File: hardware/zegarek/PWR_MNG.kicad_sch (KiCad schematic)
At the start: 14 parts, among them J1 Conn_01x02_Socket, J2 Conn_01x02_Pin, Q1 IRF740, U1 MC34063AD

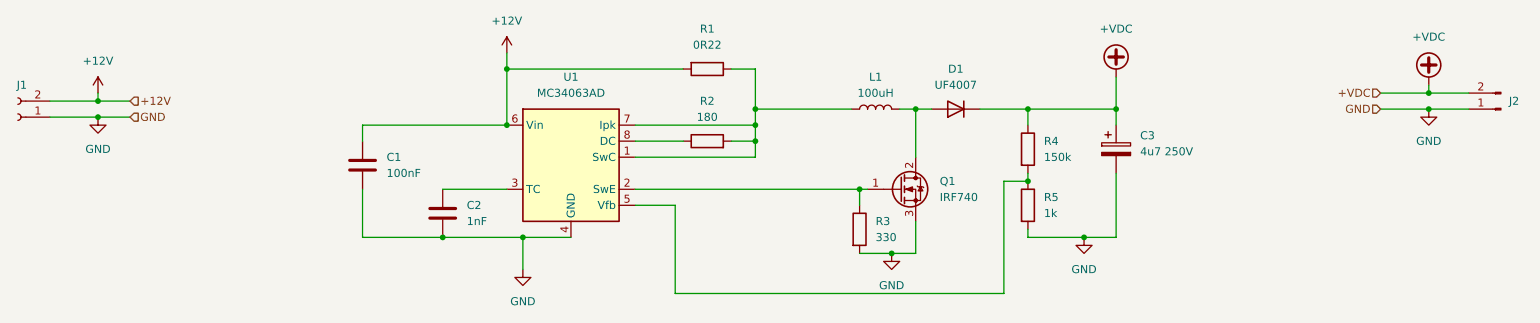
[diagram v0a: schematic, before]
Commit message: page MCU and NIXIE done, nixiepwr changed name to PWR MNG
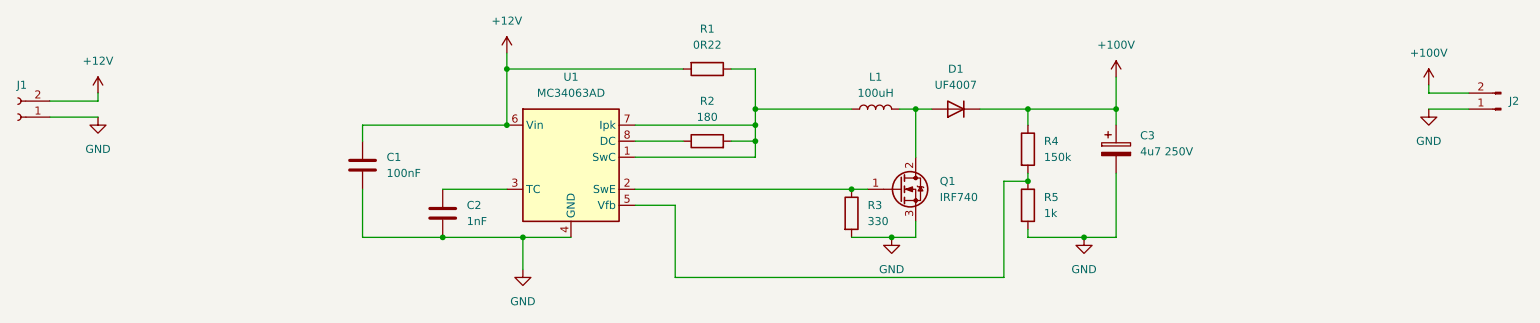
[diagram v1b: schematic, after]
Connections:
- net +VDC renamed +100V
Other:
- moved on the sheet: R3

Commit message: pwr page done
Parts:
- removed J1: Conn_01x02_Socket, Connector:Banana_Jack_2Pin, symbol Connector:Conn_01x02_Socket
- added C22, C25: 0.33u, symbol Device:C_Small
- added C23, C24: 100n, symbol Device:C_Small
- added J6: Barrel_Jack_MountingPin, Connector_BarrelJack:BarrelJack_Wuerth_694106106102_2.0x5.5mm, symbol Connector:Barrel_Jack_MountingPin
- added U8: DI78L3.3UAB, Package_TO_SOT_SMD:SOT-89-3, symbol Regulator_Linear:HT75xx-1-SOT89
- added U9: L7805ACV, Package_TO_SOT_THT:TO-220-3_Vertical, symbol Regulator_Linear:LF50_TO220
- C3: symbol Device:C_Polarized -> Device:C_Small_US
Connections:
- net +12V: now also C22.1, C25.1, J6.1, U8.2 (VIN), U9.1 (VI)
- net GND: now also C22.2, C23.2, C24.2, C25.2, J6.2, U8.1 (GND), U9.2 (GND)
- new net +3V3: C24.1, U8.3 (VOUT)
- new net +5V: C23.1, U9.3 (VO)
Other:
- moved on the sheet: C1, C2, D1, J2, L1, Q1, R1, R2, R3, R4, R5, U1

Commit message: added status leds buttons and buzzer, 100V header deleted, footprints assigned
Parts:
- removed J2: Conn_01x02_Pin, Connector:Banana_Jack_2Pin, symbol Connector:Conn_01x02_Pin
- C22, C23, C24, C25: footprint (none) -> Capacitor_SMD:C_1206_3216Metric_Pad1.33x1.80mm_HandSolder
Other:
- moved on the sheet: J6

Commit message: done placing footprins on pcb, started tracing pcb
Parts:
- J1: renamed from J6; footprint Connector_BarrelJack:BarrelJack_Wuerth_694106106102_2.0x5.5mm -> Connector_BarrelJack:BarrelJack_CUI_PJ-079BH_Horizontal
- R10: renamed from R3; footprint Resistor_SMD:R_0805_2012Metric_Pad1.20x1.40mm_HandSolder -> Resistor_SMD:R_0603_1608Metric_Pad0.98x0.95mm_HandSolder
- R11: renamed from R4; footprint Resistor_SMD:R_0805_2012Metric_Pad1.20x1.40mm_HandSolder -> Resistor_SMD:R_0603_1608Metric_Pad0.98x0.95mm_HandSolder
- R12: renamed from R5; footprint Resistor_SMD:R_0805_2012Metric_Pad1.20x1.40mm_HandSolder -> Resistor_SMD:R_0603_1608Metric_Pad0.98x0.95mm_HandSolder
- R8: renamed from R1; footprint Resistor_SMD:R_1206_3216Metric_Pad1.30x1.75mm_HandSolder -> Resistor_SMD:R_0603_1608Metric_Pad0.98x0.95mm_HandSolder
- R9: renamed from R2; footprint Resistor_SMD:R_0805_2012Metric -> Resistor_SMD:R_0603_1608Metric_Pad0.98x0.95mm_HandSolder
- renumbered C3 to C10, C25 to C4, C24 to C5, C1 to C6, C2 to C7, C22 to C8, C23 to C9, U8 to U1, U1 to U2, U9 to U3

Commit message: jlc generated bom and grb+drill
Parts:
- C4, C8: LCSC (none) -> C274377
- C5, C6, C9: LCSC (none) -> C152824
- C7: LCSC (none) -> C49326757
- D1: LCSC (none) -> C54426167
- L1: LCSC (none) -> C2045483
- Q1: footprint Package_TO_SOT_THT:TO-220-3_Vertical -> Package_TO_SOT_THT:TO-220-3_Horizontal_TabUp; LCSC (none) -> C358408
- R10: LCSC (none) -> C23138
- R11: LCSC (none) -> C22807
- R12: LCSC (none) -> C2074140
- R8: footprint Resistor_SMD:R_0603_1608Metric_Pad0.98x0.95mm_HandSolder -> Resistor_SMD:R_1206_3216Metric_Pad1.30x1.75mm_HandSolder
- R9: footprint Resistor_SMD:R_0603_1608Metric_Pad0.98x0.95mm_HandSolder -> Resistor_SMD:R_1206_3216Metric_Pad1.30x1.75mm_HandSolder; LCSC (none) -> C17924
- U2: LCSC (none) -> C2873086
- U3: footprint Package_TO_SOT_THT:TO-220-3_Vertical -> Package_TO_SOT_THT:TO-220-3_Horizontal_TabUp; LCSC (none) -> C192854
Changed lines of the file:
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@@
+			)
+		)
+		(property "LCSC" "C2045483"
+			(at 161.29 76.2 0)
+			(effects
+				(font
+					(size 1.27 1.27)
+				)
+				(hide yes)
 			)
 		)
@@
 			)
 		)
+		(property "LCSC" "C23138"
+			(at 160.02 96.5199 0)
+			(effects
+				(font
+					(size 1.27 1.27)
+				)
+				(hide yes)
+			)
+		)
 		(pin "2"
 		)
@@
 			)
 		)
-		(property "Footprint" "Resistor_SMD:R_0603_1608Metric_Pad0.98x0.95mm_HandSolder"
+		(property "Footprint" "Resistor_SMD:R_1206_3216Metric_Pad1.30x1.75mm_HandSolder"
 			(at 134.62 88.138 90)
 			(hide yes)
@@
 			)
 		)
+		(property "LCSC" "C17924"
+			(at 134.62 80.01 0)
+			(effects
+				(font
+					(size 1.27 1.27)
+				)
+				(hide yes)
+			)
+		)
 		(pin "2"
 		)
@@
 			)
 		)
+		(property "LCSC" "C152824"
+			(at 63.5 154.9462 0)
+			(effects
+				(font
+					(size 1.27 1.27)
+				)
+				(hide yes)
+			)
+		)
 		(pin "2"
 		)
@@
 			)
 		)
+		(property "LCSC" "C152824"
+			(at 149.86 153.6762 0)
+			(effects
+				(font
+					(size 1.27 1.27)
+				)
+				(hide yes)
+			)
+		)
 		(pin "2"
 		)
@@
 			)
 		)
+		(property "LCSC" "C22807"
+			(at 187.96 86.3599 0)
+			(effects
+				(font
+					(size 1.27 1.27)
+				)
+				(hide yes)
+			)
+		)
 		(pin "2"
 		)
@@
 			)
 		)
+		(property "LCSC" "C2873086"
+			(at 113.03 76.2 0)
+			(effects
+				(font
+					(size 1.27 1.27)
+				)
+				(hide yes)
+			)
+		)
 		(pin "8"
 		)
@@
 			)
 		)
+		(property "LCSC" "C54426167"
+			(at 173.99 74.93 0)
+			(effects
+				(font
+					(size 1.27 1.27)
+				)
+				(hide yes)
+			)
+		)
 		(pin "1"
 		)
@@
 			)
 		)
+		(property "LCSC" "C2074140"
+			(at 187.96 95.2499 0)
+			(effects
+				(font
+					(size 1.27 1.27)
+				)
+				(hide yes)
+			)
+		)
 		(pin "2"
 		)
@@
 			)
 		)
-		(property "Footprint" "Package_TO_SOT_THT:TO-220-3_Vertical"
+		(property "Footprint" "Package_TO_SOT_THT:TO-220-3_Horizontal_TabUp"
 			(at 170.18 95.885 0)
 			(hide yes)
@@
 			)
 		)
+		(property "LCSC" "C358408"
+			(at 171.45 92.7099 0)
+			(effects
+				(font
+					(size 1.27 1.27)
+				)
+				(hide yes)
+			)
+		)
 		(pin "1"
 		)
@@
 			)
 		)
+		(property "LCSC" "C152824"
+			(at 83.82 88.8999 0)
+			(effects
+				(font
+					(size 1.27 1.27)
+				)
+				(hide yes)
+			)
+		)
 		(pin "1"
 		)
@@
 			)
 		)
-		(property "Footprint" "Resistor_SMD:R_0603_1608Metric_Pad0.98x0.95mm_HandSolder"
+		(property "Footprint" "Resistor_SMD:R_1206_3216Metric_Pad1.30x1.75mm_HandSolder"
 			(at 134.62 73.152 90)
 			(hide yes)
@@
 			)
 		)
+		(property "LCSC" "C49326757"
+			(at 96.52 96.5199 0)
+			(effects
+				(font
+					(size 1.27 1.27)
+				)
+				(hide yes)
+			)
+		)
 		(pin "1"
 		)
@@
 			)
 		)
-		(property "Footprint" "Package_TO_SOT_THT:TO-220-3_Vertical"
+		(property "Footprint" "Package_TO_SOT_THT:TO-220-3_Horizontal_TabUp"
 			(at 134.62 145.415 0)
 			(hide yes)
@@
 			)
 		)
+		(property "LCSC" "C192854"
+			(at 134.62 144.78 0)
+			(effects
+				(font
+					(size 1.27 1.27)
+				)
+				(hide yes)
+			)
+		)
 		(pin "3"
 		)
@@
 			)
 		)
+		(property "LCSC" "C274377"
+			(at 33.02 154.9462 0)
+			(effects
+				(font
+					(size 1.27 1.27)
+				)
+				(hide yes)
+			)
+		)
 		(pin "2"
 		)
@@
 			)
 		)
+		(property "LCSC" "C274377"
+			(at 119.38 153.6762 0)
+			(effects
+				(font
+					(size 1.27 1.27)
+				)
+				(hide yes)
+			)
+		)

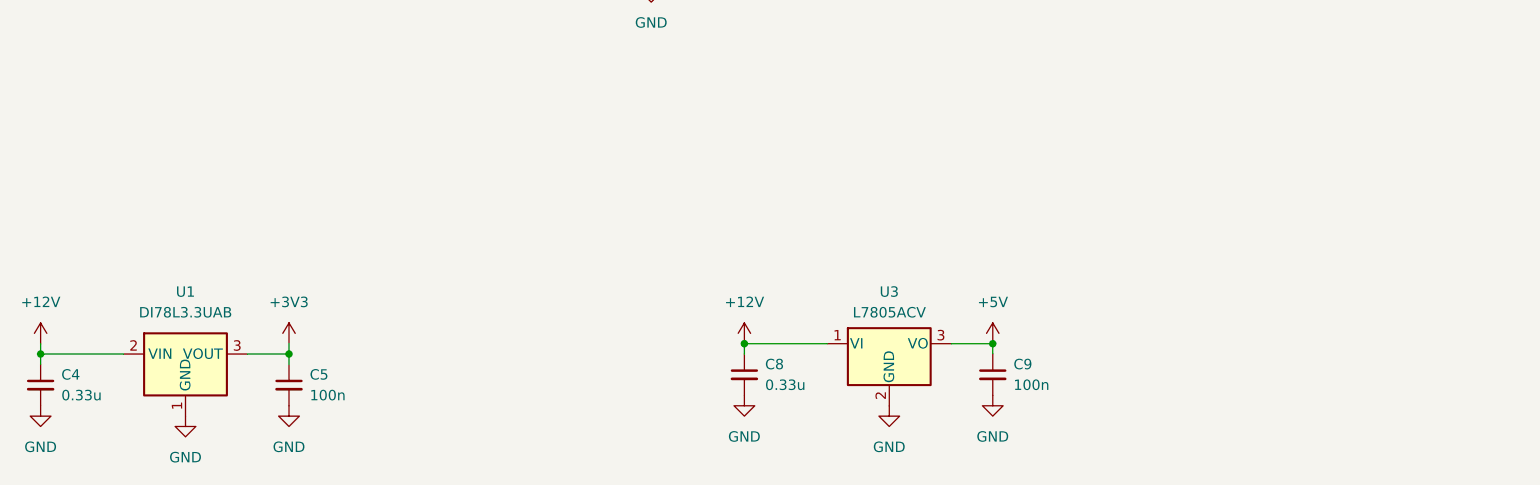
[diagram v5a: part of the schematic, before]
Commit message: new revision with fixes from prototype: level shift to mcu added, changed con footprints and debug usb deleted
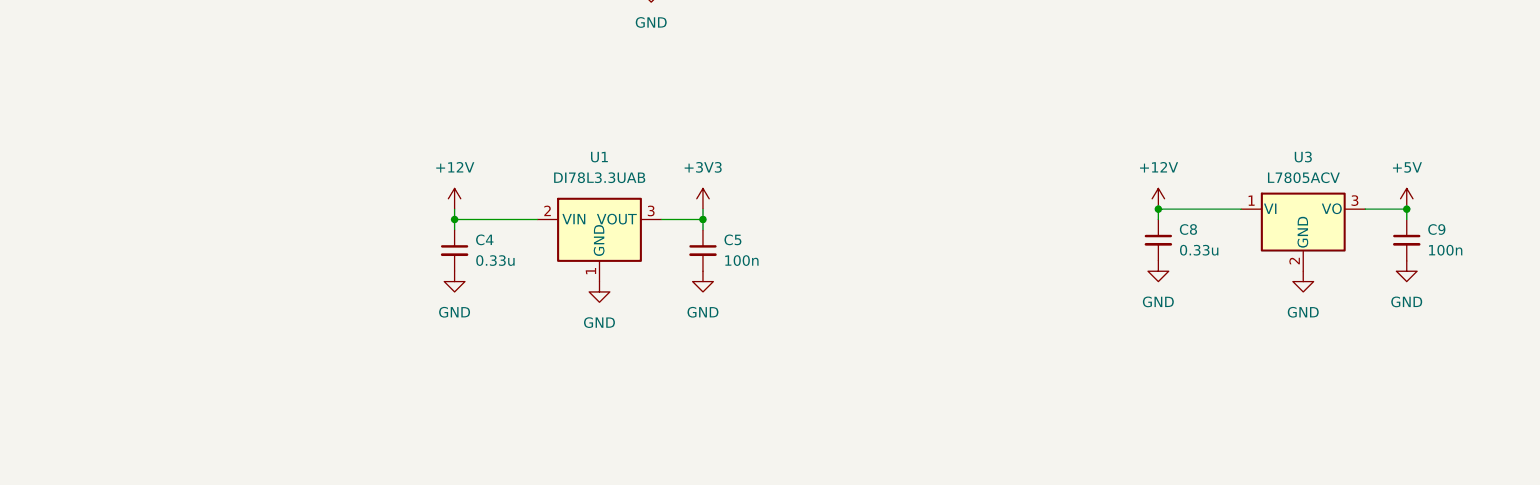
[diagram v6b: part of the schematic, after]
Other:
- moved on the sheet: C4, C5, C8, C9, U1, U3

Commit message: rerouting tubes order for proper display order
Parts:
- J1: footprint Connector_BarrelJack:BarrelJack_CUI_PJ-079BH_Horizontal -> Connector_BarrelJack:BarrelJack_GCT_DCJ200-10-A_Horizontal
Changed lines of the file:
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@@
 			)
 		)
-		(property "Footprint" "Connector_BarrelJack:BarrelJack_CUI_PJ-079BH_Horizontal"
+		(property "Footprint" "Connector_BarrelJack:BarrelJack_GCT_DCJ200-10-A_Horizontal"
 			(at 132.08 40.386 0)
 			(hide yes)

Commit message: reqenerating postprod
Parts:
- added C24: 100u, Capacitor_SMD:C_1206_3216Metric_Pad1.33x1.80mm_HandSolder, symbol Device:C_Polarized_Small
- added F1: Fuse, Fuse:Fuse_1812_4532Metric_Pad1.30x3.40mm_HandSolder, symbol Device:Fuse
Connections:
- net +12V: now also C24.1, F1.2; no longer J1.1
- net GND: now also C24.2
- new net: F1.1, J1.1
